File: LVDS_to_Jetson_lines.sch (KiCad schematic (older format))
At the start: 0 parts

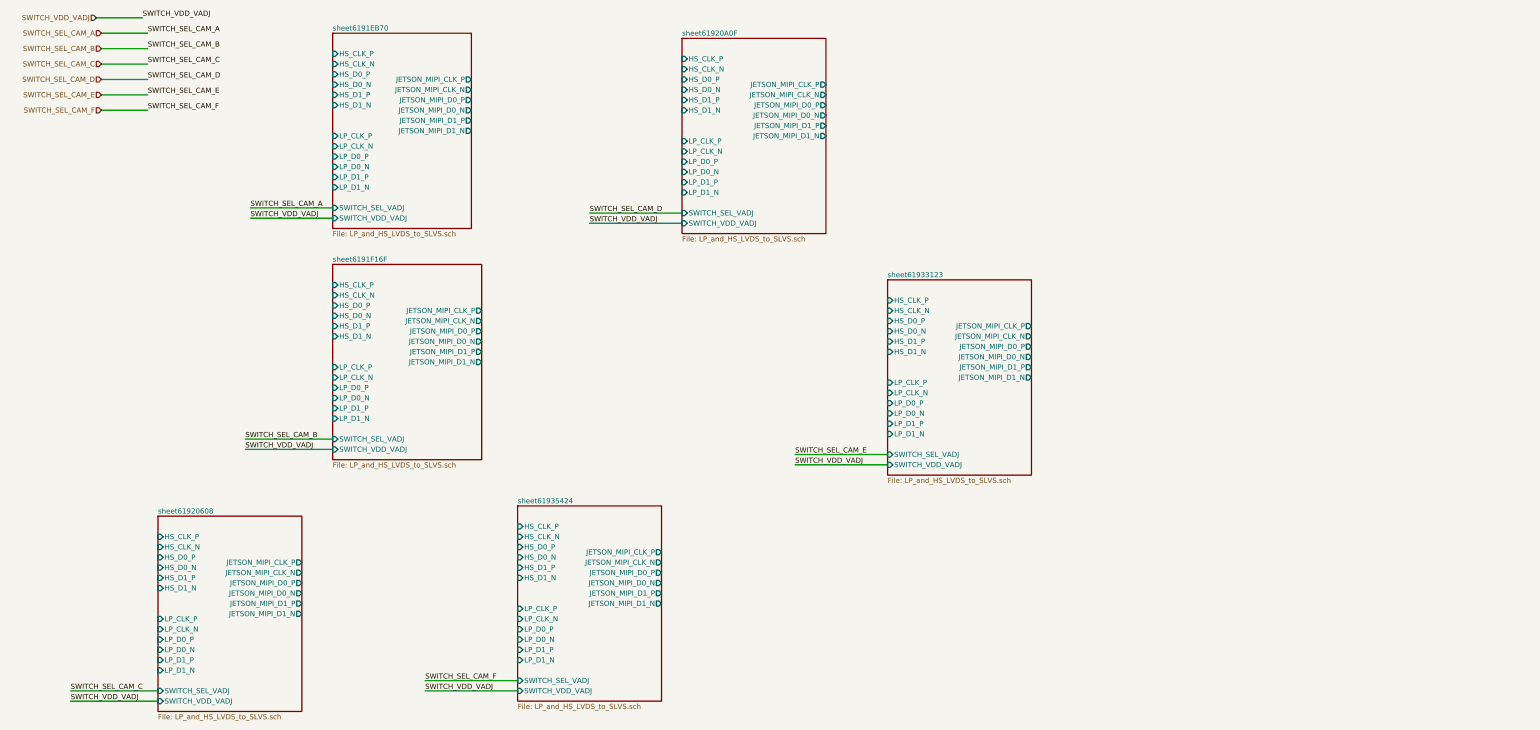
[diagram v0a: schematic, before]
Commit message: Good, before replacing the swithches to TI ones
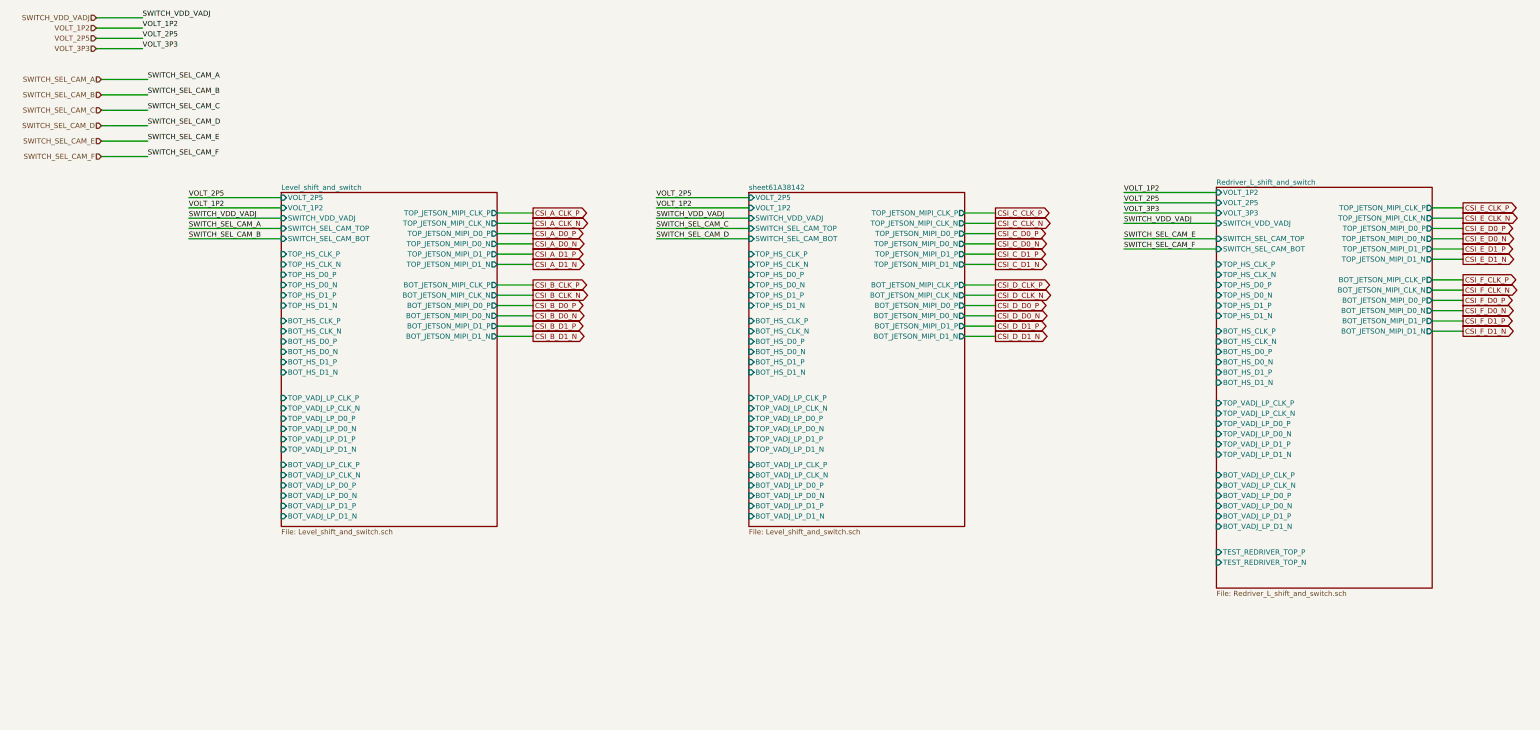
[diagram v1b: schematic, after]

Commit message: good, added re-driver
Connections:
- net labels added: VDD_VADJ
- net labels removed: SWITCH_VDD_VADJ
- wire segments 62 -> 50
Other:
- note added: "TODO: Not mandatory, but good idea to add level shifters to SWITCH_HS_0_LP_1_3V3_3V3\nhttp://cdn.sparkfun.com/datasheets/BreakoutBoards/Logic_Level_Bidirectional.pdf\nTest it!!"

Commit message: good, before reducing
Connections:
- net labels added: SWITCH_CAM_C_D
- net labels removed: SWITCH_SEL_CAM_A
- wire segments 50 -> 51
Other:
- note removed: "TODO: Not mandatory, but good idea to add level shifters to SWITCH_HS_0_LP_1_3V3_3V3\nhttp://cdn.sparkfun.com/datasheets/BreakoutBoards/Logic_Level_Bidirectional.pdf\nTest it!!"
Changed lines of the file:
@@
 $Descr A3 16535 11693
 encoding utf-8
-Sheet 4 7
+Sheet 4 15
 Title ""
 Date ""
@@
 VDD_VADJ
 Text HLabel 1350 1250 0    50   Input ~ 0
-SWITCH_SEL_CAM_A
+SWITCH_CAM_C_D
 Wire Wire Line
 	1350 1250 1800 1250
 Text Label 1800 1250 0    50   ~ 0
-SWITCH_SEL_CAM_A
+SWITCH_CAM_C_D
 Text HLabel 1350 1400 0    50   Input ~ 0
 SWITCH_SEL_CAM_B
@@
 Text Label 1750 950  0    50   ~ 0
 VOLT_3P3
-Text GLabel 10050 3450 2    50   Output ~ 0
+Text GLabel 5500 3450 2    50   Output ~ 0
 CSI_D_D0_P
-Text GLabel 10050 3550 2    50   Output ~ 0
+Text GLabel 5500 3550 2    50   Output ~ 0
 CSI_D_D0_N
-Text GLabel 10050 3250 2    50   Output ~ 0
+Text GLabel 5500 3250 2    50   Output ~ 0
 CSI_D_CLK_P
-Text GLabel 10050 3350 2    50   Output ~ 0
+Text GLabel 5500 3350 2    50   Output ~ 0
 CSI_D_CLK_N
-Text GLabel 10050 3650 2    50   Output ~ 0
+Text GLabel 5500 3650 2    50   Output ~ 0
 CSI_D_D1_P
-Text GLabel 10050 3750 2    50   Output ~ 0
+Text GLabel 5500 3750 2    50   Output ~ 0
 CSI_D_D1_N
 Text GLabel 15150 3450 2    50   Output ~ 0
@@
 Text GLabel 15150 3750 2    50   Output ~ 0
 CSI_F_D1_N
-Text GLabel 10050 2750 2    50   Output ~ 0
+Text GLabel 5500 2750 2    50   Output ~ 0
 CSI_C_D0_P
-Text GLabel 10050 2850 2    50   Output ~ 0
+Text GLabel 5500 2850 2    50   Output ~ 0
 CSI_C_D0_N
-Text GLabel 10050 2550 2    50   Output ~ 0
+Text GLabel 5500 2550 2    50   Output ~ 0
 CSI_C_CLK_P
-Text GLabel 10050 2650 2    50   Output ~ 0
+Text GLabel 5500 2650 2    50   Output ~ 0
 CSI_C_CLK_N
-Text GLabel 10050 2950 2    50   Output ~ 0
+Text GLabel 5500 2950 2    50   Output ~ 0
 CSI_C_D1_P
-Text GLabel 10050 3050 2    50   Output ~ 0
+Text GLabel 5500 3050 2    50   Output ~ 0
 CSI_C_D1_N
 Text GLabel 15150 2750 2    50   Output ~ 0
@@
 CSI_E_D1_N
 Wire Wire Line
-	9750 2550 10050 2550
-Wire Wire Line
-	9750 2650 10050 2650
-Wire Wire Line
-	9750 2750 10050 2750
-Wire Wire Line
-	9750 2850 10050 2850
-Wire Wire Line
-	9750 2950 10050 2950
-Wire Wire Line
-	9750 3050 10050 3050
-Wire Wire Line
-	9750 3250 10050 3250
-Wire Wire Line
-	9750 3350 10050 3350
-Wire Wire Line
-	9750 3450 10050 3450
-Wire Wire Line
-	9750 3550 10050 3550
-Wire Wire Line
-	9750 3650 10050 3650
-Wire Wire Line
-	9750 3750 10050 3750
+	5200 2550 5500 2550
+Wire Wire Line
+	5200 2650 5500 2650
+Wire Wire Line
+	5200 2750 5500 2750
+Wire Wire Line
+	5200 2850 5500 2850
+Wire Wire Line
+	5200 2950 5500 2950
+Wire Wire Line
+	5200 3050 5500 3050
+Wire Wire Line
+	5200 3250 5500 3250
+Wire Wire Line
+	5200 3350 5500 3350
+Wire Wire Line
+	5200 3450 5500 3450
+Wire Wire Line
+	5200 3550 5500 3550
+Wire Wire Line
+	5200 3650 5500 3650
+Wire Wire Line
+	5200 3750 5500 3750
 Wire Wire Line
 	2200 2700 3100 2700
@@
 Wire Wire Line
 	2200 2600 3100 2600
-Text Notes 2900 2150 0    50   ~ 0
-TODO: Not mandatory, but good idea to add level shifters to SWITCH_HS_0_LP_1_3V3_3V3\nhttp://cdn.sparkfun.com/datasheets/BreakoutBoards/Logic_Level_Bidirectional.pdf\nTest it!!
 Wire Wire Line
 	14700 2550 15150 2550
@@
 F39 "BOT_VADJ_LP_D1_N" I L 3100 5500 50
 F40 "VOLT_2P5" I L 3100 2400 50
-F41 "SWITCH_HS_0_LP_1_3V3" I L 3100 2800 50
+F41 "SWITCH_HS_0_LP_1_VADJ" I L 3100 2800 50
 F42 "VOLT_3P3" I L 3100 2600 50
 $EndSheet
-Text GLabel 5500 3550 2    50   Output ~ 0
+Text GLabel 8650 3500 2    50   Output ~ 0
 CSI_B_D0_N
-Text GLabel 5500 3450 2    50   Output ~ 0
+Text GLabel 8650 3400 2    50   Output ~ 0
 CSI_B_D0_P
-Text GLabel 5500 2750 2    50   Output ~ 0
+Text GLabel 8650 2700 2    50   Output ~ 0
 CSI_A_D0_P
-Text GLabel 5500 2850 2    50   Output ~ 0
+Text GLabel 8650 2800 2    50   Output ~ 0
 CSI_A_D0_N
-Text GLabel 5500 2650 2    50   Output ~ 0
+Text GLabel 8650 2600 2    50   Output ~ 0
 CSI_A_CLK_N
-Text GLabel 5500 2550 2    50   Output ~ 0
+Text GLabel 8650 2500 2    50   Output ~ 0
 CSI_A_CLK_P
-Text GLabel 5500 3050 2    50   Output ~ 0
+Text GLabel 8650 3000 2    50   Output ~ 0
 CSI_A_D1_N
-Text GLabel 5500 2950 2    50   Output ~ 0
+Text GLabel 8650 2900 2    50   Output ~ 0
 CSI_A_D1_P
-Text GLabel 5500 3350 2    50   Output ~ 0
+Text GLabel 8650 3300 2    50   Output ~ 0
 CSI_B_CLK_N
-Text GLabel 5500 3250 2    50   Output ~ 0
+Text GLabel 8650 3200 2    50   Output ~ 0
 CSI_B_CLK_P
-Text GLabel 5500 3750 2    50   Output ~ 0
+Text GLabel 8650 3700 2    50   Output ~ 0
 CSI_B_D1_N
-Text GLabel 5500 3650 2    50   Output ~ 0
+Text GLabel 8650 3600 2    50   Output ~ 0
 CSI_B_D1_P
 Wire Wire Line
-	5200 2550 5500 2550
-Wire Wire Line
-	5200 2650 5500 2650
-Wire Wire Line
-	5200 2750 5500 2750
-Wire Wire Line
-	5200 2850 5500 2850
-Wire Wire Line
-	5200 2950 5500 2950
-Wire Wire Line
-	5200 3050 5500 3050
-Wire Wire Line
-	5200 3250 5500 3250
-Wire Wire Line
-	5200 3350 5500 3350
-Wire Wire Line
-	5200 3450 5500 3450
-Wire Wire Line
-	5200 3550 5500 3550
-Wire Wire Line
-	5200 3650 5500 3650
-Wire Wire Line
-	5200 3750 5500 3750
+	8350 2500 8650 2500
+Wire Wire Line
+	8350 2600 8650 2600
+Wire Wire Line
+	8350 2700 8650 2700
+Wire Wire Line
+	8350 2800 8650 2800
+Wire Wire Line
+	8350 2900 8650 2900
+Wire Wire Line
+	8350 3000 8650 3000
+Wire Wire Line
+	8350 3200 8650 3200
+Wire Wire Line
+	8350 3300 8650 3300
+Wire Wire Line
+	8350 3400 8650 3400
+Wire Wire Line
+	8350 3500 8650 3500
+Wire Wire Line
+	8350 3600 8650 3600
+Wire Wire Line
+	8350 3700 8650 3700
+Text Label 2200 2800 0    50   ~ 0
+SWITCH_CAM_C_D
+Wire Wire Line
+	3100 2800 2200 2800
 $EndSCHEMATC

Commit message: before re-arranging
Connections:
- net labels added: SWITCH_HS_LV_CAM_C
- net labels removed: SWITCH_CAM_C_D, SWITCH_SEL_CAM_B, SWITCH_SEL_CAM_C, SWITCH_SEL_CAM_D, SWITCH_SEL_CAM_E, SWITCH_SEL_CAM_F
- wire segments 51 -> 47
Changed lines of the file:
@@
 VDD_VADJ
 Text HLabel 1350 1250 0    50   Input ~ 0
-SWITCH_CAM_C_D
+SWITCH_HS_LV_CAM_C
 Wire Wire Line
 	1350 1250 1800 1250
 Text Label 1800 1250 0    50   ~ 0
-SWITCH_CAM_C_D
-Text HLabel 1350 1400 0    50   Input ~ 0
-SWITCH_SEL_CAM_B
-Wire Wire Line
-	1350 1400 1800 1400
-Text Label 1800 1400 0    50   ~ 0
-SWITCH_SEL_CAM_B
-Text HLabel 1350 1550 0    50   Input ~ 0
-SWITCH_SEL_CAM_C
-Wire Wire Line
-	1350 1550 1800 1550
-Text Label 1800 1550 0    50   ~ 0
-SWITCH_SEL_CAM_C
-Text HLabel 1350 1700 0    50   Input ~ 0
-SWITCH_SEL_CAM_D
-Wire Wire Line
-	1350 1700 1800 1700
-Text Label 1800 1700 0    50   ~ 0
-SWITCH_SEL_CAM_D
-Text HLabel 1350 1850 0    50   Input ~ 0
-SWITCH_SEL_CAM_E
-Wire Wire Line
-	1350 1850 1800 1850
-Text Label 1800 1850 0    50   ~ 0
-SWITCH_SEL_CAM_E
-Text HLabel 1350 2000 0    50   Input ~ 0
-SWITCH_SEL_CAM_F
-Wire Wire Line
-	1350 2000 1800 2000
-Text Label 1800 2000 0    50   ~ 0
-SWITCH_SEL_CAM_F
+SWITCH_HS_LV_CAM_C
 Text HLabel 1300 750  0    50   Input ~ 0
 VOLT_1P2
@@
 Text Label 1750 950  0    50   ~ 0
 VOLT_3P3
-Text GLabel 5500 3450 2    50   Output ~ 0
+Text GLabel 9500 3950 2    50   Output ~ 0
 CSI_D_D0_P
-Text GLabel 5500 3550 2    50   Output ~ 0
+Text GLabel 9500 4050 2    50   Output ~ 0
 CSI_D_D0_N
-Text GLabel 5500 3250 2    50   Output ~ 0
+Text GLabel 9500 3750 2    50   Output ~ 0
 CSI_D_CLK_P
-Text GLabel 5500 3350 2    50   Output ~ 0
+Text GLabel 9500 3850 2    50   Output ~ 0
 CSI_D_CLK_N
-Text GLabel 5500 3650 2    50   Output ~ 0
+Text GLabel 9500 4150 2    50   Output ~ 0
 CSI_D_D1_P
-Text GLabel 5500 3750 2    50   Output ~ 0
+Text GLabel 9500 4250 2    50   Output ~ 0
 CSI_D_D1_N
 Text GLabel 15150 3450 2    50   Output ~ 0
@@
 	5200 3050 5500 3050
 Wire Wire Line
-	5200 3250 5500 3250
-Wire Wire Line
-	5200 3350 5500 3350
-Wire Wire Line
-	5200 3450 5500 3450
-Wire Wire Line
-	5200 3550 5500 3550
-Wire Wire Line
-	5200 3650 5500 3650
-Wire Wire Line
-	5200 3750 5500 3750
+	9200 3750 9500 3750
+Wire Wire Line
+	9200 3850 9500 3850
+Wire Wire Line
+	9200 3950 9500 3950
+Wire Wire Line
+	9200 4050 9500 4050
+Wire Wire Line
+	9200 4150 9500 4150
+Wire Wire Line
+	9200 4250 9500 4250
 Wire Wire Line
 	2200 2700 3100 2700
@@
 Wire Wire Line
 	14700 3750 15150 3750
+Text Label 2200 2800 0    50   ~ 0
+SWITCH_HS_LV_CAM_C
+Wire Wire Line
+	3100 2800 2200 2800
 $Sheet
 S 3100 2350 2100 3250
 U 61A814B9
-F0 "Level_shift_and_switch" 50
-F1 "Level_shift_and_switch.sch" 50
+F0 "Level_shift_and_switch_single" 50
+F1 "Level_shift_and_switch_single.sch" 50
 F2 "VDD_VADJ" I L 3100 2700 50
 F3 "VOLT_1P2" I L 3100 2500 50
-F4 "BOT_JT_MIPI_CLK_P" O R 5200 3250 50
-F5 "BOT_JT_MIPI_CLK_N" O R 5200 3350 50
-F6 "TOP_JT_MIPI_D1_P" O R 5200 2950 50
-F7 "TOP_JT_MIPI_D1_N" O R 5200 3050 50
-F8 "BOT_JT_MIPI_D1_P" O R 5200 3650 50
-F9 "BOT_JT_MIPI_D1_N" O R 5200 3750 50
-F10 "BOT_JT_MIPI_D0_P" O R 5200 3450 50
-F11 "BOT_JT_MIPI_D0_N" O R 5200 3550 50
-F12 "TOP_JT_MIPI_D0_P" O R 5200 2750 50
-F13 "TOP_JT_MIPI_D0_N" O R 5200 2850 50
-F14 "TOP_JT_MIPI_CLK_P" O R 5200 2550 50
-F15 "TOP_JT_MIPI_CLK_N" O R 5200 2650 50
-F16 "TOP_HS_CLK_P" I L 3100 2950 50
-F17 "TOP_HS_CLK_N" I L 3100 3050 50
-F18 "TOP_HS_D0_P" I L 3100 3150 50
-F19 "TOP_HS_D0_N" I L 3100 3250 50
-F20 "TOP_HS_D1_P" I L 3100 3350 50
-F21 "TOP_HS_D1_N" I L 3100 3450 50
-F22 "BOT_HS_CLK_P" I L 3100 3600 50
-F23 "BOT_HS_CLK_N" I L 3100 3700 50
-F24 "BOT_HS_D0_P" I L 3100 3800 50
-F25 "BOT_HS_D0_N" I L 3100 3900 50
-F26 "BOT_HS_D1_P" I L 3100 4000 50
-F27 "BOT_HS_D1_N" I L 3100 4100 50
-F28 "TOP_VADJ_LP_CLK_P" I L 3100 4350 50
-F29 "TOP_VADJ_LP_CLK_N" I L 3100 4450 50
-F30 "TOP_VADJ_LP_D0_P" I L 3100 4550 50
-F31 "TOP_VADJ_LP_D0_N" I L 3100 4650 50
-F32 "TOP_VADJ_LP_D1_P" I L 3100 4750 50
-F33 "TOP_VADJ_LP_D1_N" I L 3100 4850 50
-F34 "BOT_VADJ_LP_CLK_P" I L 3100 5000 50
-F35 "BOT_VADJ_LP_CLK_N" I L 3100 5100 50
-F36 "BOT_VADJ_LP_D0_P" I L 3100 5200 50
-F37 "BOT_VADJ_LP_D0_N" I L 3100 5300 50
-F38 "BOT_VADJ_LP_D1_P" I L 3100 5400 50
-F39 "BOT_VADJ_LP_D1_N" I L 3100 5500 50
-F40 "VOLT_2P5" I L 3100 2400 50
-F41 "SWITCH_HS_0_LP_1_VADJ" I L 3100 2800 50
-F42 "VOLT_3P3" I L 3100 2600 50
+F4 "TOP_JT_MIPI_D1_P" O R 5200 2950 50
+F5 "TOP_JT_MIPI_D1_N" O R 5200 3050 50
+F6 "TOP_JT_MIPI_D0_P" O R 5200 2750 50
+F7 "TOP_JT_MIPI_D0_N" O R 5200 2850 50
+F8 "TOP_JT_MIPI_CLK_P" O R 5200 2550 50
+F9 "TOP_JT_MIPI_CLK_N" O R 5200 2650 50
+F10 "TOP_HS_CLK_P" I L 3100 2950 50
+F11 "TOP_HS_CLK_N" I L 3100 3050 50
+F12 "TOP_HS_D0_P" I L 3100 3150 50
+F13 "TOP_HS_D0_N" I L 3100 3250 50
+F14 "TOP_HS_D1_P" I L 3100 3350 50
+F15 "TOP_HS_D1_N" I L 3100 3450 50
+F16 "TOP_VADJ_LP_CLK_P" I L 3100 4350 50
+F17 "TOP_VADJ_LP_CLK_N" I L 3100 4450 50
+F18 "TOP_VADJ_LP_D0_P" I L 3100 4550 50
+F19 "TOP_VADJ_LP_D0_N" I L 3100 4650 50
+F20 "TOP_VADJ_LP_D1_P" I L 3100 4750 50
+F21 "TOP_VADJ_LP_D1_N" I L 3100 4850 50
+F22 "VOLT_2P5" I L 3100 2400 50
+F23 "SWITCH_HS_0_LP_1_VADJ" I L 3100 2800 50
+F24 "VOLT_3P3" I L 3100 2600 50
+F25 "RDR_TST_P" I L 3100 3750 50
+F26 "RDR_TST_N" I L 3100 3850 50
 $EndSheet
-Text GLabel 8650 3500 2    50   Output ~ 0
+Text GLabel 12800 6550 2    50   Output ~ 0
+CSI_A_D0_P
+Text GLabel 12800 6650 2    50   Output ~ 0
+CSI_A_D0_N
+Text GLabel 12800 6450 2    50   Output ~ 0
+CSI_A_CLK_N
+Text GLabel 12800 6350 2    50   Output ~ 0
+CSI_A_CLK_P
+Text GLabel 12800 6850 2    50   Output ~ 0
+CSI_A_D1_N
+Text GLabel 12800 6750 2    50   Output ~ 0
+CSI_A_D1_P
+Text GLabel 12800 6550 2    50   Output ~ 0
+CSI_A_D0_P
+Text GLabel 12800 6650 2    50   Output ~ 0
+CSI_A_D0_N
+Text GLabel 12800 6450 2    50   Output ~ 0
+CSI_A_CLK_N
+Text GLabel 12800 6350 2    50   Output ~ 0
+CSI_A_CLK_P
+Text GLabel 12800 6850 2    50   Output ~ 0
+CSI_A_D1_N
+Text GLabel 12800 6750 2    50   Output ~ 0
+CSI_A_D1_P
+Text GLabel 9450 2900 2    50   Output ~ 0
 CSI_B_D0_N
-Text GLabel 8650 3400 2    50   Output ~ 0
+Text GLabel 9450 2800 2    50   Output ~ 0
 CSI_B_D0_P
-Text GLabel 8650 2700 2    50   Output ~ 0
-CSI_A_D0_P
-Text GLabel 8650 2800 2    50   Output ~ 0
-CSI_A_D0_N
-Text GLabel 8650 2600 2    50   Output ~ 0
-CSI_A_CLK_N
-Text GLabel 8650 2500 2    50   Output ~ 0
-CSI_A_CLK_P
-Text GLabel 8650 3000 2    50   Output ~ 0
-CSI_A_D1_N
-Text GLabel 8650 2900 2    50   Output ~ 0
-CSI_A_D1_P
-Text GLabel 8650 3300 2    50   Output ~ 0
+Text GLabel 9450 2700 2    50   Output ~ 0
 CSI_B_CLK_N
-Text GLabel 8650 3200 2    50   Output ~ 0
+Text GLabel 9450 2600 2    50   Output ~ 0
 CSI_B_CLK_P
-Text GLabel 8650 3700 2    50   Output ~ 0
+Text GLabel 9450 2500 2    50   Output ~ 0
 CSI_B_D1_N
-Text GLabel 8650 3600 2    50   Output ~ 0
+Text GLabel 9450 2400 2    50   Output ~ 0
 CSI_B_D1_P
 Wire Wire Line
-	8350 2500 8650 2500
-Wire Wire Line
-	8350 2600 8650 2600
-Wire Wire Line
-	8350 2700 8650 2700
-Wire Wire Line
-	8350 2800 8650 2800
-Wire Wire Line
-	8350 2900 8650 2900
-Wire Wire Line
-	8350 3000 8650 3000
-Wire Wire Line
-	8350 3200 8650 3200
-Wire Wire Line
-	8350 3300 8650 3300
-Wire Wire Line
-	8350 3400 8650 3400
-Wire Wire Line
-	8350 3500 8650 3500
-Wire Wire Line
-	8350 3600 8650 3600
-Wire Wire Line
-	8350 3700 8650 3700
-Text Label 2200 2800 0    50   ~ 0
-SWITCH_CAM_C_D
-Wire Wire Line
-	3100 2800 2200 2800
+	9150 2700 9450 2700
+Wire Wire Line
+	9150 2600 9450 2600
+Wire Wire Line
+	9150 2900 9450 2900
+Wire Wire Line
+	9150 2800 9450 2800
+Wire Wire Line
+	9150 2500 9450 2500
+Wire Wire Line
+	9150 2400 9450 2400
+Wire Wire Line
+	8950 6200 8300 6200
+Text Label 8300 6200 0    50   ~ 0
+VOLT_2P5
+Wire Wire Line
+	12150 6850 12800 6850
+Wire Wire Line
+	12150 6750 12800 6750
+Wire Wire Line
+	12150 6450 12800 6450
+Wire Wire Line
+	12150 6350 12800 6350
+Wire Wire Line
+	12150 6650 12800 6650
+Wire Wire Line
+	12150 6550 12800 6550
+$Sheet
+S 8950 6100 3200 1100
+U 61D68977
+F0 "LVDS_to_Jetson_simple" 50
+F1 "LVDS_to_Jetson_simple.sch" 50
+F2 "VOLT_2P5" I L 8950 6200 50
+F3 "EXP_CLK_P" O R 12150 6350 50
+F4 "EXP_CLK_N" O R 12150 6450 50
+F5 "EXP_D1_P" O R 12150 6750 50
+F6 "EXP_D1_N" O R 12150 6850 50
+F7 "EXP_D0_P" O R 12150 6550 50
+F8 "EXP_D0_N" O R 12150 6650 50
+$EndSheet
 $EndSCHEMATC

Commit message: rev 2022
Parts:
- added C14, C15, C16, C17, C18, C19, C20, C21, C22, C23: 0.1uF, Capacitors_SMD:C_0402, symbol FMC_MIPI_v2:C
- added R37, R38: 0, Resistors_SMD:R_0805, symbol Device:R
- added U5, U6: TS3DDR3812_RUA_42, FMC_MIPI_v2_sym:TS3DDR3812RUAR, symbol FMC_MIPI_v2:TS3DDR3812_RUA_42
- added U8: SN74AVCH16T245_DGV_48, FMC_MIPI_v2_sym:DGV48, symbol FMC_MIPI_v2:SN74AVCH16T245_DGV_48
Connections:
- net labels added: EN, Earth, FMC_HS_CSI_C_CLK_N, FMC_HS_CSI_C_CLK_P, FMC_HS_CSI_C_D0_N, FMC_HS_CSI_C_D0_P, FMC_HS_CSI_C_D1_N, FMC_HS_CSI_C_D1_P, FMC_HS_CSI_D_CLK_N, FMC_HS_CSI_D_CLK_P, FMC_HS_CSI_D_D0_N, FMC_HS_CSI_D_D0_P, FMC_HS_CSI_D_D1_N, FMC_HS_CSI_D_D1_P, HS_CSI_C_CLK_N, HS_CSI_C_CLK_P, HS_CSI_C_D0_N, HS_CSI_C_D0_P, HS_CSI_C_D1_N, HS_CSI_C_D1_P, HS_CSI_D_CLK_N, HS_CSI_D_CLK_P, HS_CSI_D_D0_N, HS_CSI_D_D0_P, HS_CSI_D_D1_N, HS_CSI_D_D1_P, LP_CSI_C_CLK_N, LP_CSI_C_CLK_P, LP_CSI_C_D0_N, LP_CSI_C_D0_P, LP_CSI_C_D1_N, LP_CSI_C_D1_P, LP_CSI_D_CLK_N, LP_CSI_D_CLK_P, LP_CSI_D_D0_N, LP_CSI_D_D0_P, LP_CSI_D_D1_N, LP_CSI_D_D1_P, fdmkls_TOP_VADJ_LP_CLK_N, fdmkls_TOP_VADJ_LP_CLK_P, fdmkls_TOP_VADJ_LP_D0_N, fdmkls_TOP_VADJ_LP_D0_P, fdmkls_TOP_VADJ_LP_D1_N, fdmkls_TOP_VADJ_LP_D1_P
- wire segments 47 -> 250
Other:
- note added: "BUG: use CSI A and CSI B from the same IC, since they can form 4 lane configuration\n"
- note added: "Decoupling capacitors U5"
- note added: "Decoupling capacitors U6"
- note added: "HS Lanes"
- note added: "LP lanes"
- note added: "LP/HS switch clock lanes"
- note added: "LP/HS switch data lanes"
- note added: "Level shifting"
- note added: "Note: HS and clock lanes has a separate switch IC's, this is for tow reasons:\n1) Enable shorter LP state for clock lanes, as required in D-PHY standard\n2) Enable continious mode for clock"
- note added: "Note: LP signal are single ended!! No need to treat them as diffrential,\n+ they are low speed, so SI is not an issue.\nPlacing it at the bottom layer for now."
- note added: "TODO: check level shifting with FPGA when OE and DIR are tied to ground without resistor"
